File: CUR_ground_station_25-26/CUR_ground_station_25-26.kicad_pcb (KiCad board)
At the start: 4 copper layers, 74 x 58.6 mm, 84 parts, among them J1 Conn_01x02, J2 UJ20-C-H-G-SMT-P16-TR, J3 Conn_Coaxial_Small, J4 Conn_01x04_Pin, Q1 NTR4003N, Q2 NTR4003N, SW1 PTS815SJM250SMTRLFS, SW2 PTS815SJM250SMTRLFS, SW3 PTS815SJM250SMTRLFS, SW4 PTS815SJM250SMTRLFS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

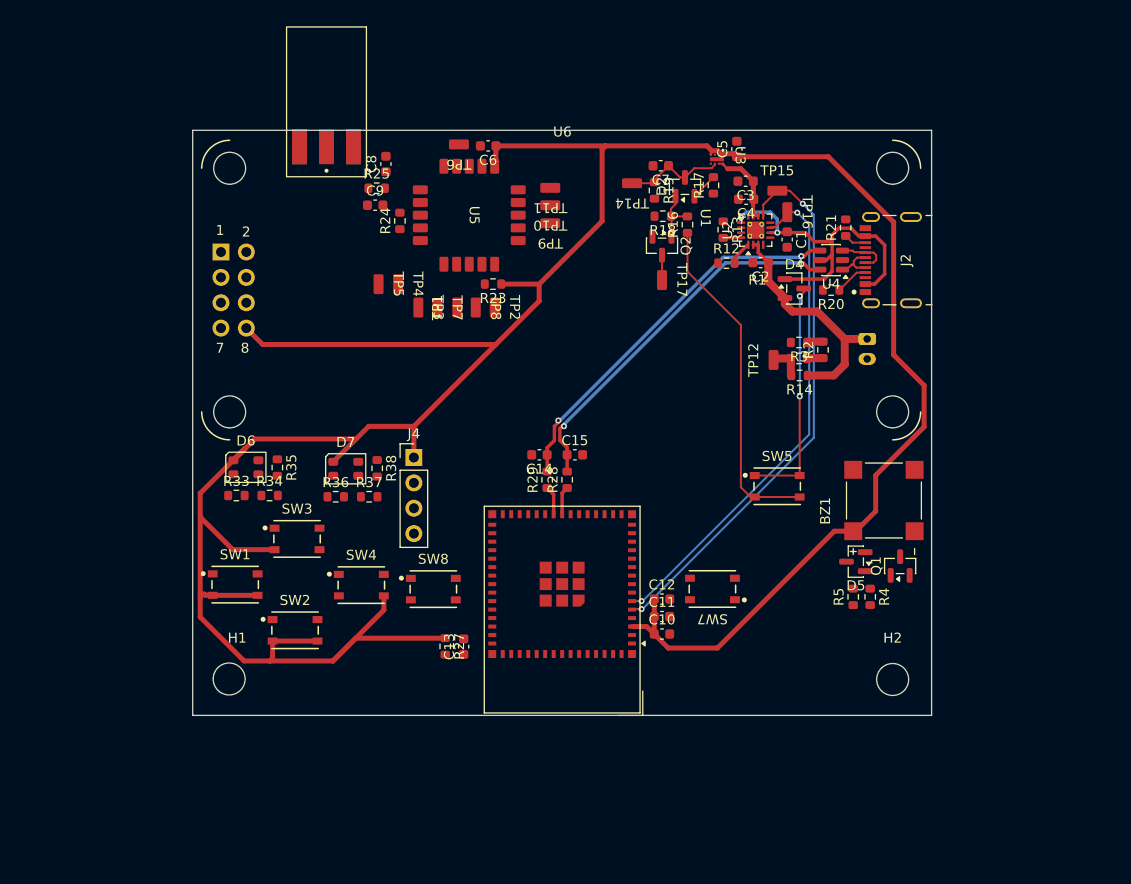
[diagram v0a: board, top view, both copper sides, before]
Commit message: changed to four layer board
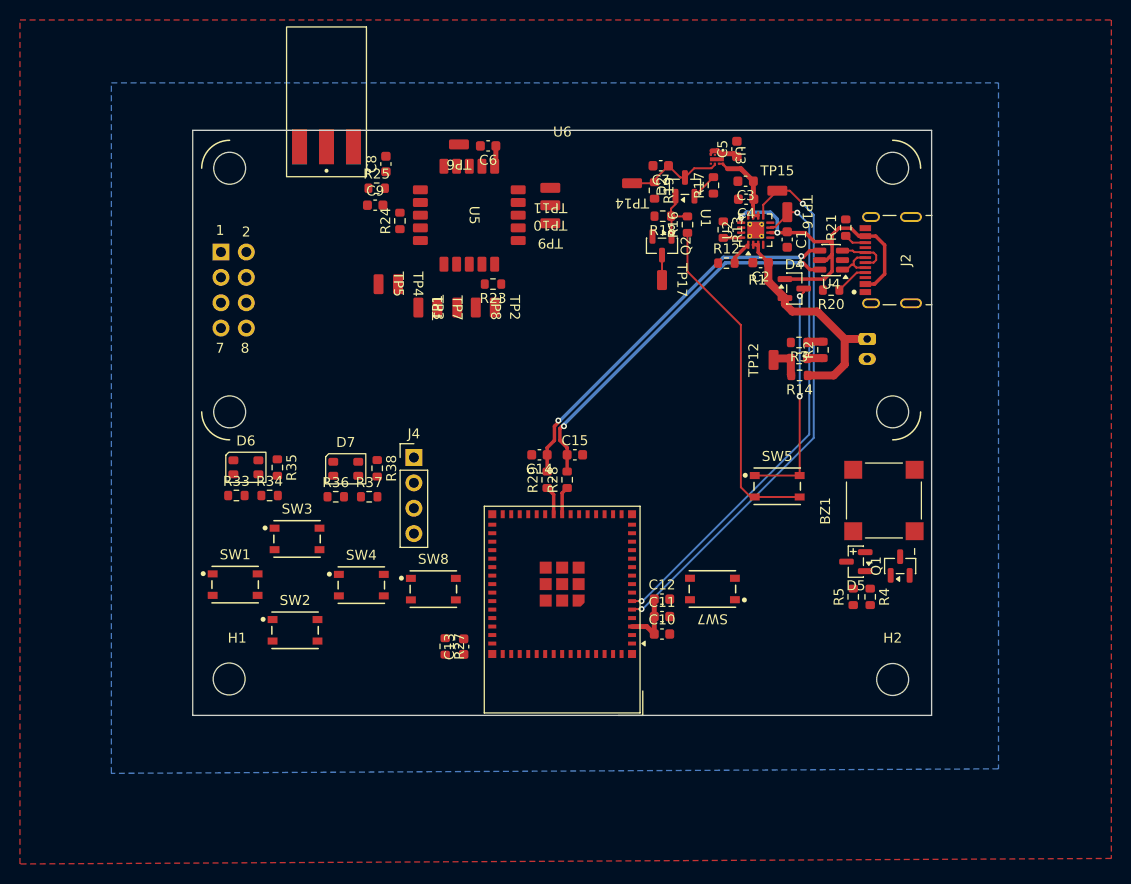
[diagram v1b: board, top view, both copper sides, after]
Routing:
- net +3V3: track 279.6 -> 11.5 mm
- added copper zone on In2.Cu, net +3V3
- added copper zone on B.Cu, net GND
- added copper zone on F.Cu, net GND
- added copper zone on In1.Cu, net GND

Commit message: signal routing
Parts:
- moved Q1 9.22 mm to (110.8, 97.2), turned to 0 degrees
- moved R4 8.95 mm to (107.8, 94.2), turned to 180 degrees
- moved BZ1 8.55 mm to (117.7, 95.6), turned to 0 degrees
- moved R5 8.08 mm to (107.8, 92.5), turned to 0 degrees
- moved J4 6.97 mm to (72.5, 89.5), turned to -90 degrees
- moved C12 5.07 mm to (99.1, 100.5), turned to -90 degrees
- moved SW7 4.86 mm to (103.2, 100.0)
- moved D5 3.65 mm to (111.3, 92.8), turned to 90 degrees
- moved SW4 2.57 mm to (66.2, 98.0)
- moved C11 2.43 mm to (97.1, 100.5), turned to -90 degrees
- moved SW1 2.39 mm to (53.6, 97.7)
- moved SW2 2.39 mm to (59.6, 102.3)
- moved SW3 2.39 mm to (59.8, 93.1)
- moved SW8 2.01 mm to (73.4, 97.8)
- moved R27 1.36 mm to (75.0, 102.3), turned to 0 degrees
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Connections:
- U1 pad 10: /MCU/BUZZER -> /MCU/PWR_BTN
- U1 pad 11: /MCU/RF_IO1 -> /MCU/RF_IO3
- U1 pad 13: /MCU/RF_IO3 -> /MCU/RF_IO1
- U1 pad 20: /MCU/LED_1_R -> /MCU/LED_2_B
- U1 pad 21: /MCU/LED_1_G -> /MCU/LED_2_G
- U1 pad 22: /MCU/LED_1_B -> /MCU/LED_2_R
- U1 pad 28: /MCU/LED_2_R -> /MCU/LED_1_R
- U1 pad 29: /MCU/LED_2_G -> /MCU/LED_1_G
- U1 pad 31: /MCU/LED_2_B -> /MCU/LED_1_B
- U1 pad 32: /MCU/DISP_D/~{C} -> /MCU/DISP_BUSY
- U1 pad 33: /MCU/DISP_CS -> /MCU/DISP_~{RES}
- U1 pad 34: /MCU/DISP_SCL -> /MCU/DISP_CS
- U1 pad 36: /MCU/DISP_BUSY -> /MCU/DISP_SCL
- U1 pad 37: /MCU/DISP_~{RES} -> /MCU/DISP_D/~{C}
- U1 pad 5: /MCU/~{CHG} -> /MCU/BUZZER
- U1 pad 6: /MCU/~{PGOOD} -> /MCU/~{CHG}
- U1 pad 7: /MCU/PWR_EN -> /MCU/~{PGOOD}
- U1 pad 8: /MCU/PWR_BTN -> /MCU/BATT_VSENSE
- U1 pad 9: /MCU/BATT_VSENSE -> /MCU/PWR_EN
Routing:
- net /MCU/DISP_D/~{C}: track 0.00 -> 50.9 mm
- net /MCU/~{RF_RESET}: track 0.00 -> 49.7 mm
- net /MCU/RF_IO3: track 0.00 -> 48.0 mm
- net /MCU/DISP_SCL: track 0.00 -> 47.1 mm
- net /MCU/RF_IO2: track 0.00 -> 45.7 mm
- net /MCU/PWR_EN: track 0.00 -> 44.2 mm
- net /MCU/DISP_BUSY: track 0.00 -> 44.1 mm
- net /MCU/RF_IO1: track 0.00 -> 42.7 mm
- net /MCU/DISP_SDA: track 0.00 -> 40.8 mm
- net /MCU/DISP_~{RES}: track 0.00 -> 40.8 mm
- net /MCU/DISP_CS: track 0.00 -> 40.1 mm
- net /MCU/LED_2_R: track 0.00 -> 39.5 mm, vias 0 -> 2
- net /MCU/RF_TXEN: track 0.00 -> 38.1 mm
- net /MCU/LED_2_B: track 0.00 -> 37.0 mm, vias 0 -> 2
- net /MCU/LED_2_G: track 0.00 -> 36.5 mm, vias 0 -> 2
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
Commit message: Update CUR_ground_station_25-26.kicad_pcb
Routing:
- net GND: track 11.6 -> 31.3 mm, vias 9 -> 30

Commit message: Update CUR_ground_station_25-26.kicad_pcb
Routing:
- net GND: track 31.3 -> 20.8 mm, vias 30 -> 44

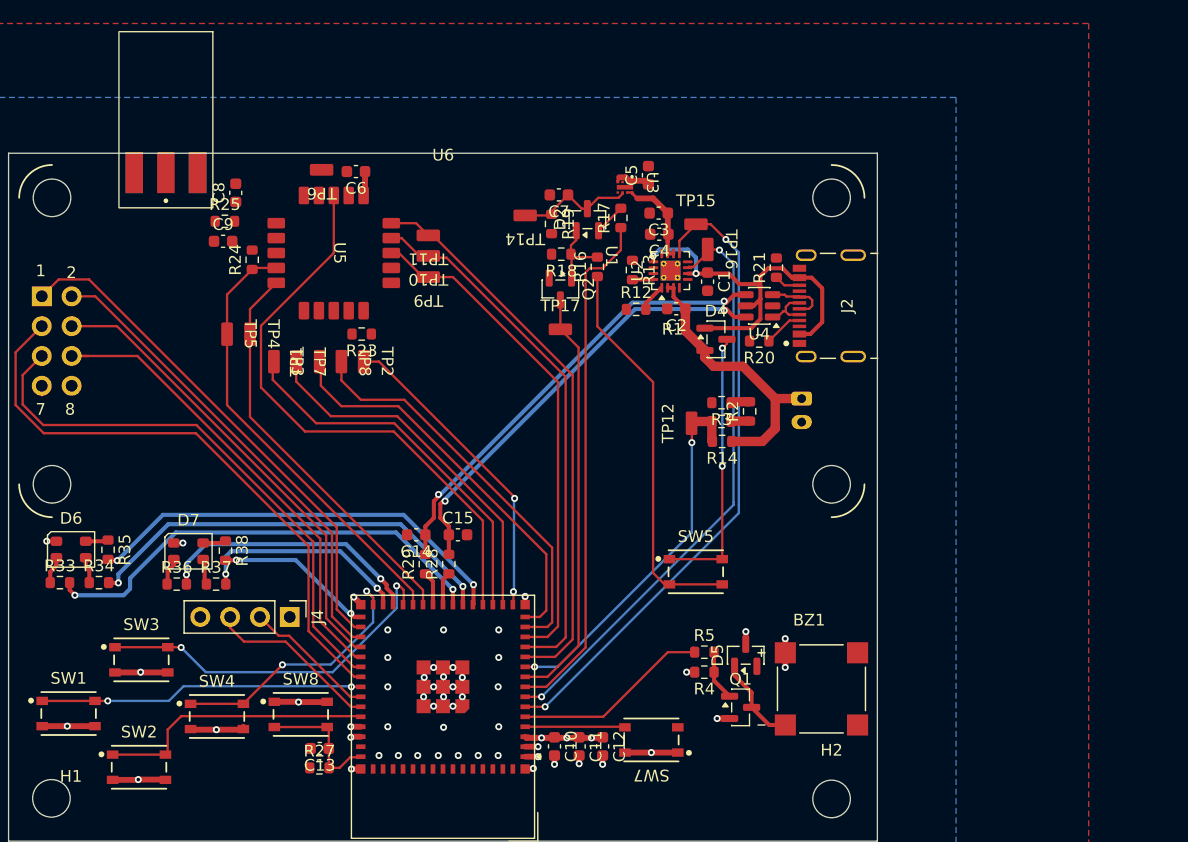
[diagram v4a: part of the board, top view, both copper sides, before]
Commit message: routing, ddrc addressed
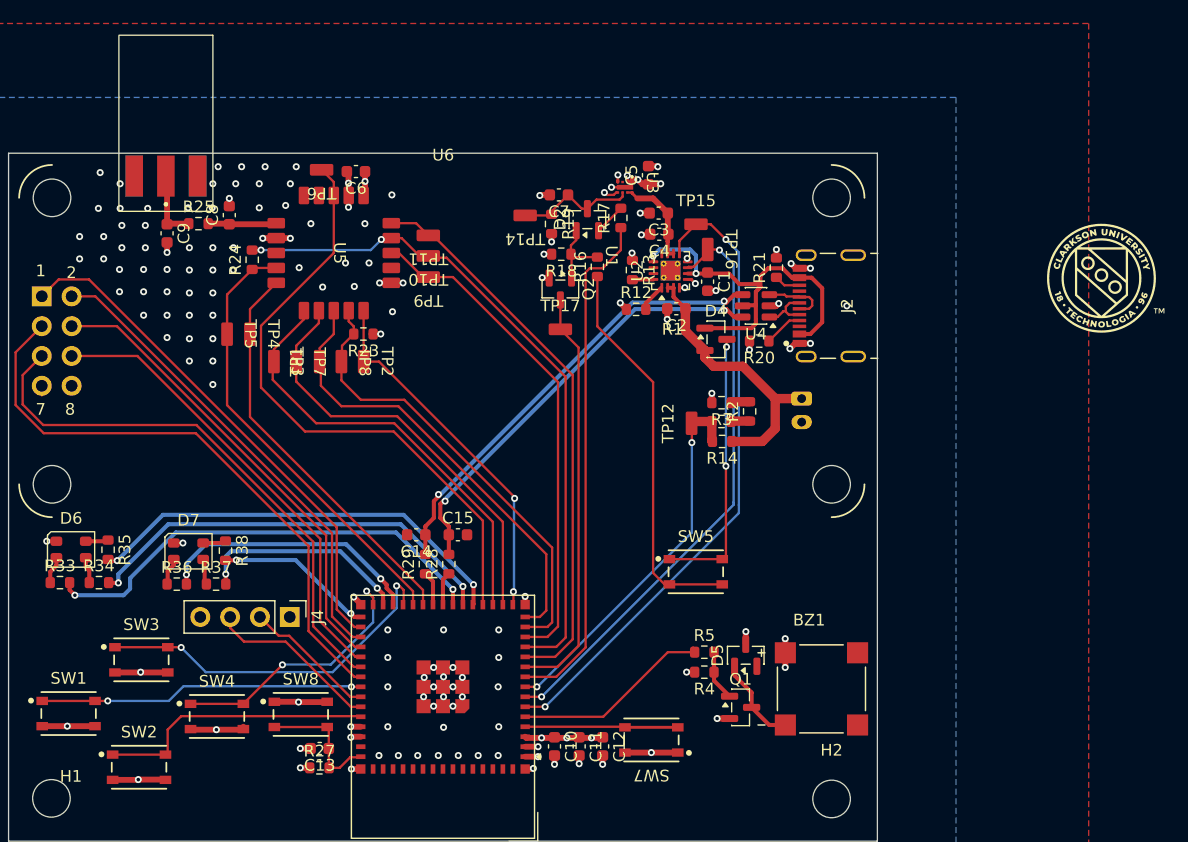
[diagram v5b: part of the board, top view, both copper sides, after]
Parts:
- added G***: LOGO, LOGO, F.Cu at (141.9, 60.6)
- added G***: LOGO, LOGO, B.Cu at (155.4, 67.3)
- moved C9 4.82 mm to (62.0, 56.8), turned to -90 degrees
- moved R25 2.26 mm to (64.7, 56.0)
- moved C8 1.98 mm to (67.3, 55.3)
- moved J3 0.30 mm to (61.9, 52.0)
- moved U4 0.28 mm to (112.2, 63.0)
- moved R23 0.15 mm to (78.7, 65.4)
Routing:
- net GND: track 20.8 -> 49.9 mm, vias 44 -> 136
- net /MCU/RF_IO2: track 45.7 -> 58.0 mm, vias 0 -> 2
- net Net-(J3-In): track 0.00 -> 6.31 mm
- net Net-(U5-ANT): track 0.00 -> 5.86 mm
- net /MCU/RF_BUSY: track 32.4 -> 37.8 mm
- net /MCU/RF_MISO: track 31.2 -> 36.4 mm
- net /MCU/~{RF_NSS}: track 34.5 -> 39.4 mm
- net /MCU/RF_MOSI: track 34.1 -> 38.9 mm
- net /MCU/RF_SCK: track 26.8 -> 31.4 mm
- net /MCU/BOOT: track 8.59 -> 13.1 mm
- net +3V3: track 34.9 -> 37.5 mm, vias 12 -> 19
- net /MCU/~{RF_RESET}: track 49.7 -> 52.3 mm
- net /MCU/DISP_SDA: track 40.8 -> 39.4 mm
- net /MCU/BATT_VSENSE: track 31.8 -> 32.5 mm
- net Net-(J2-D--PadA7): track 4.31 -> 4.86 mm
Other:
- board text added: "Clarkson University Rocketry Team 2026"

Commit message: vias place, some labeling
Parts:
- removed the G*** at (141.9, 60.6)
- removed the G*** at (155.4, 67.3)
- added G***: LOGO, LOGO, B.Cu at (100.0, 83.0)
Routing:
- net GND: vias 136 -> 193
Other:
- board text added: "(symbol "LOGO" (pin_names (offset 1.016)) (in_bom yes) (on_board yes) (property "Reference" "#G" (at 0 24.3742 0) (effects (font (size 1.27 1.27)) hide) ) (property "Value" "LOGO" (at 0 -24.3742 0) (effects (font (size 1.27 1.27)) hide) ) (property "Footprint" "" (at 0 0 0) (effects (font (size 1.27 1.27)) hide) ) (property "Datasheet" "" (at 0 0 0) (effects (font (size 1.27 1.27)) hide) ) (symbo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"
- board text added: "Clarkson University Rocketry Team Ground Station V1 - 2026"
- board text removed: "Clarkson University Rocketry Team 2026"

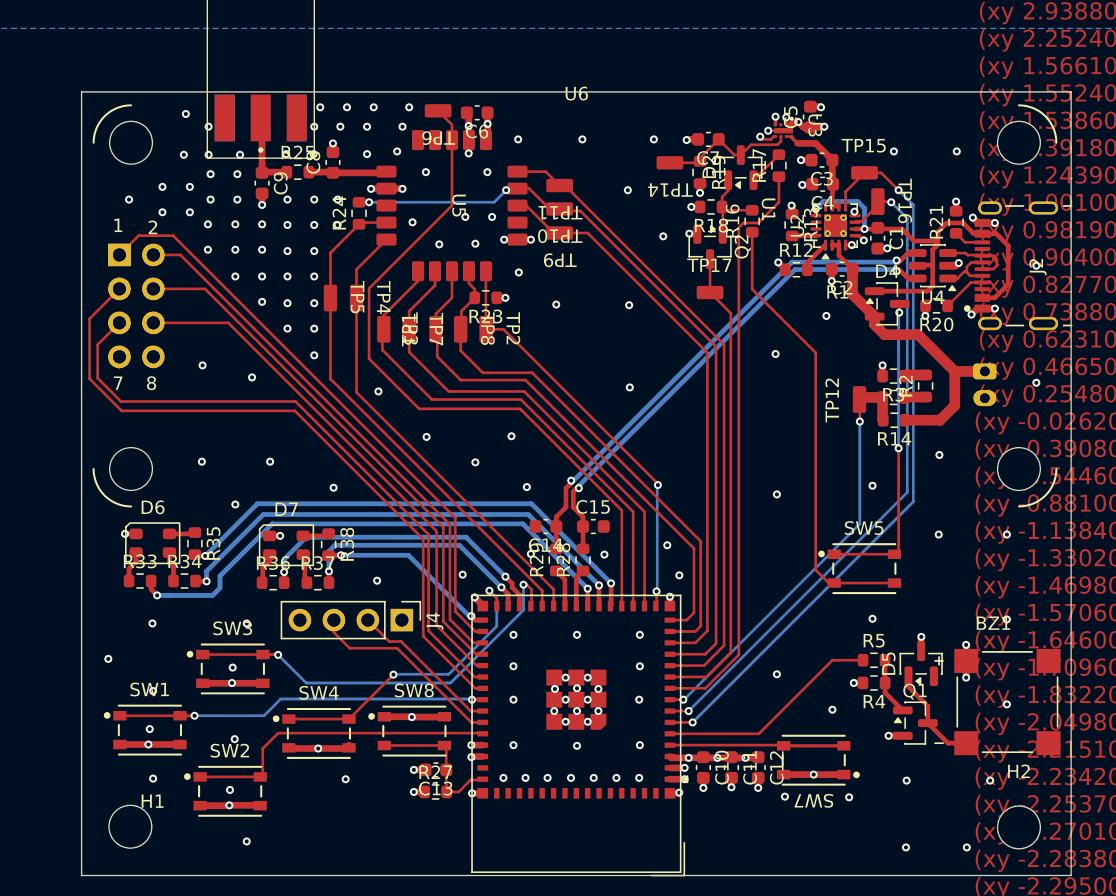
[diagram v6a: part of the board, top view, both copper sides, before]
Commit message: labing, adding gnd vias, other cleanup
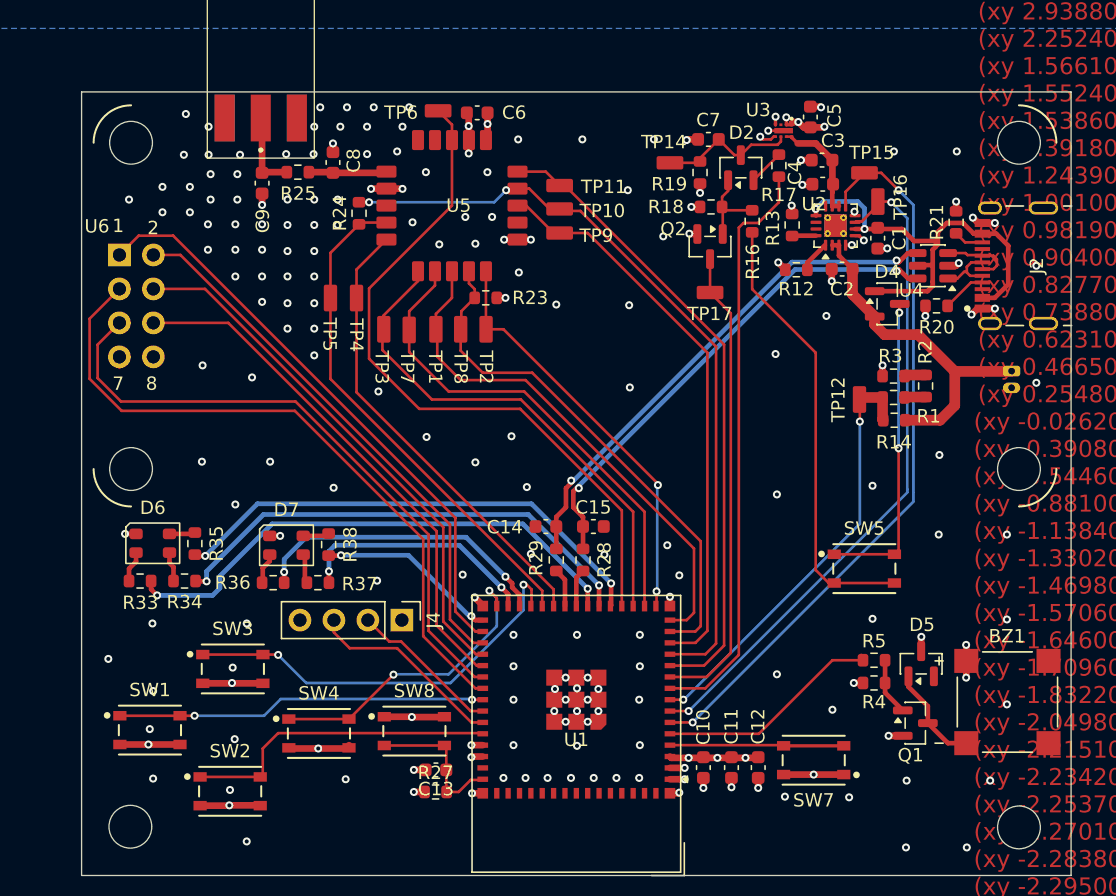
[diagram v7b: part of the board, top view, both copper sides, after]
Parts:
- J1: footprint Connector_JST:JST_PH_S2B-PH-K_1x02_P2.00mm_Horizontal -> Connector_Molex:Molex_PicoBlade_53048-0210_1x02_P1.25mm_Horizontal
- moved J1 2.00 mm to (118.0, 70.9)
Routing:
- net +BATT: track 24.1 -> 26.1 mm

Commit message: routing progress
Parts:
- added G***: LOGO, LOGO, B.Cu at (68.5, 100.4)
- moved SW5 3.92 mm to (106.5, 89.5)
- moved J4 2.00 mm to (72.5, 91.5)
- moved R38 1.39 mm to (67.3, 85.2)
- moved D7 1.39 mm to (64.2, 85.2)
- moved R33 1.39 mm to (53.2, 87.9)
- moved R37 1.39 mm to (66.5, 88.0)
- moved D6 1.39 mm to (54.1, 85.1)
- moved R34 1.39 mm to (56.5, 87.9)
- moved R35 1.39 mm to (57.3, 85.1)
- moved R36 1.39 mm to (63.1, 88.0)
- moved SW1 1.30 mm to (53.5, 99.0)
- moved SW2 1.30 mm to (59.5, 103.6)
- moved SW3 1.30 mm to (59.7, 94.4)
- moved SW4 1.30 mm to (66.2, 99.3)
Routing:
- net Net-(D4-Pad3): track 23.4 -> 27.5 mm
- net Net-(R16-Pad1): track 33.7 -> 37.4 mm
- net /MCU/UART_RX: track 14.8 -> 13.5 mm
- net /MCU/BTN_4: track 22.7 -> 24.1 mm
- net /MCU/LED_2_G: track 36.5 -> 37.7 mm
- net /MCU/LED_2_B: track 37.0 -> 38.2 mm
- net /MCU/UART_TX: track 11.4 -> 10.4 mm
- net /MCU/LED_2_R: track 39.5 -> 40.5 mm
- net /MCU/BTN_1: track 27.7 -> 28.3 mm
- net /MCU/BTN_2: track 23.6 -> 23.4 mm, vias 0 -> 2
- net GND: vias 193 -> 191
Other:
- board text added: "Thank you to"
